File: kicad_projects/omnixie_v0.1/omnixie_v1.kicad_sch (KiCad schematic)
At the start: 67 parts, among them J1 Conn_01x10, J2 SM04B-SRSS-TB, J3 SM04B-SRSS-TB, J4 USB4105-GF-A, J5 Conn_01x04, J6 Conn_01x02, J8 IL-WX-16S-VF-B-E1000E, Q0 BSS123, Q1 BSS123, Q10 BSS123, Q11 BSS123, Q12 IPN50R1K4CEATMA1, Q2 BSS123, Q3 BSS123, Q4 BSS123, Q5 BSS123, Q6 BSS123, Q7 BSS123, Q8 BSS123, Q9 BSS123, T1 ATB322515-0110, U1 CH32V003F4U6, U3 PI4IOE5V6416ZDEX, U4 XC6206P332MR

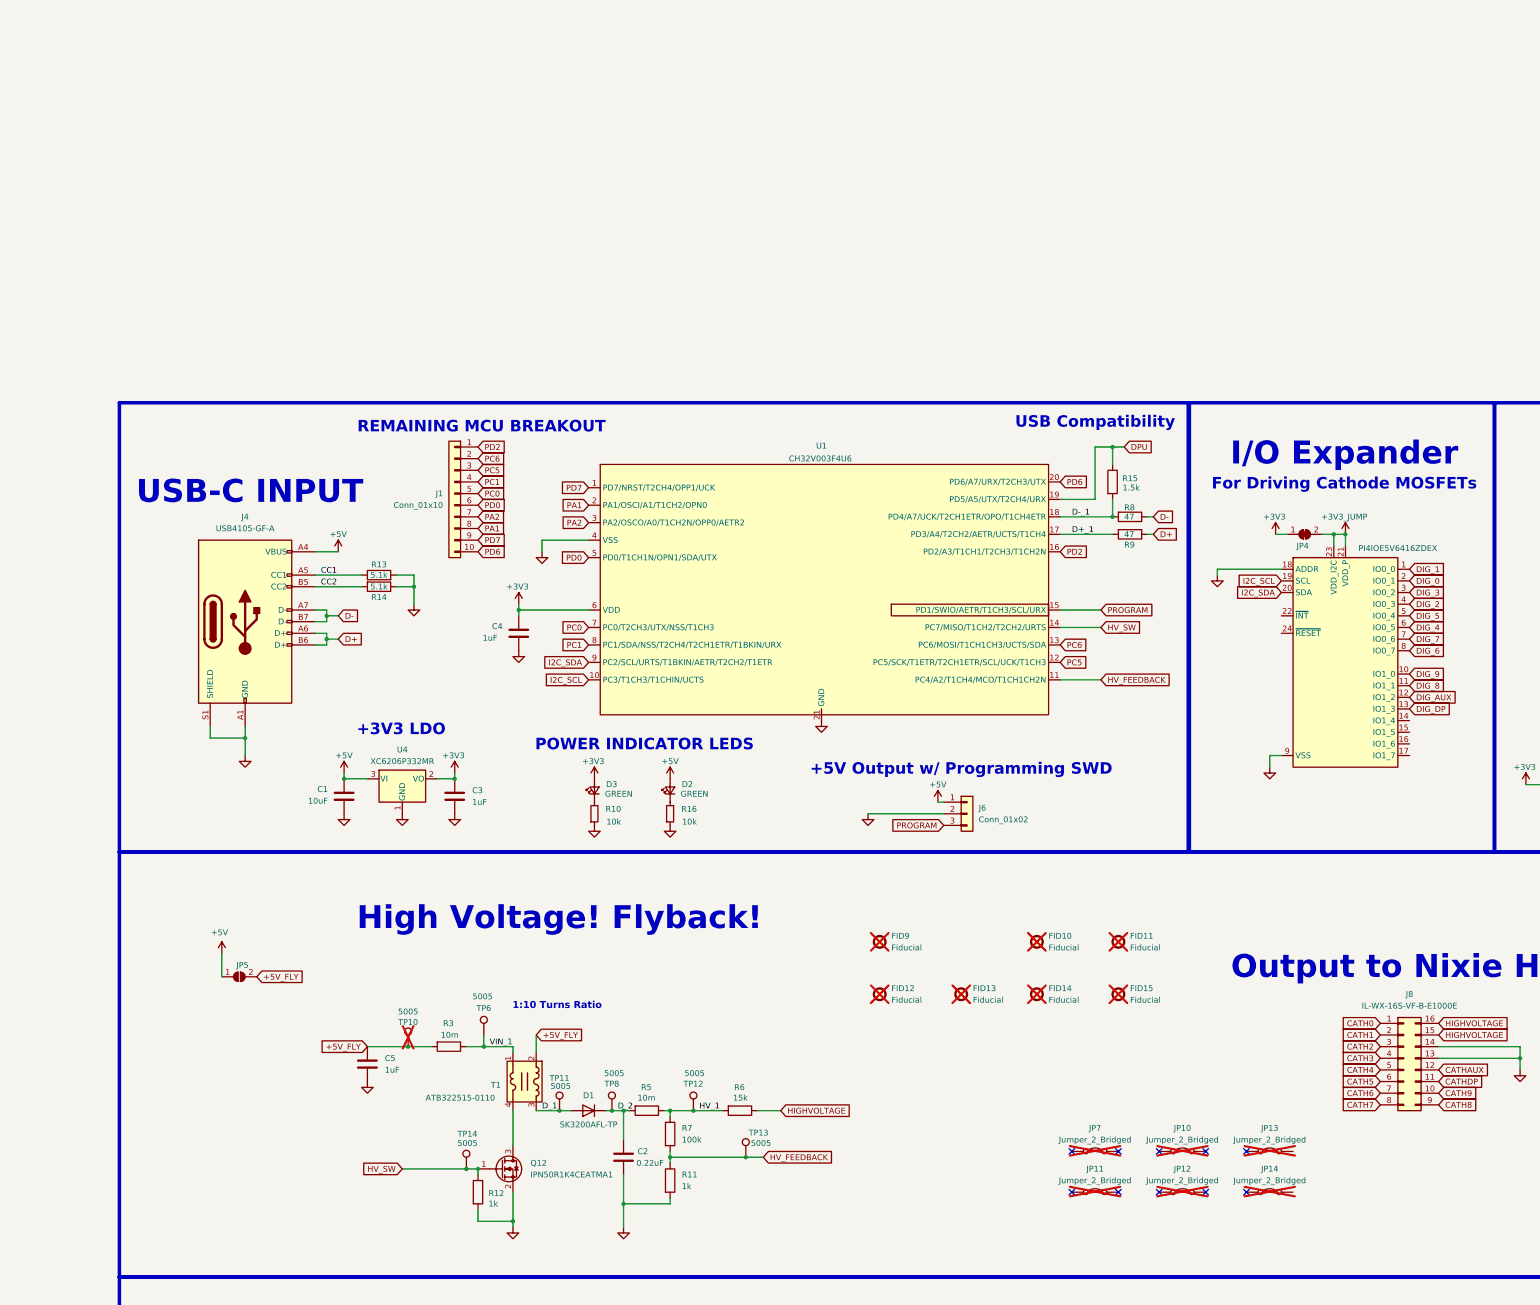
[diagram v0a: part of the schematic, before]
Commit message: removed unneccesary stuff
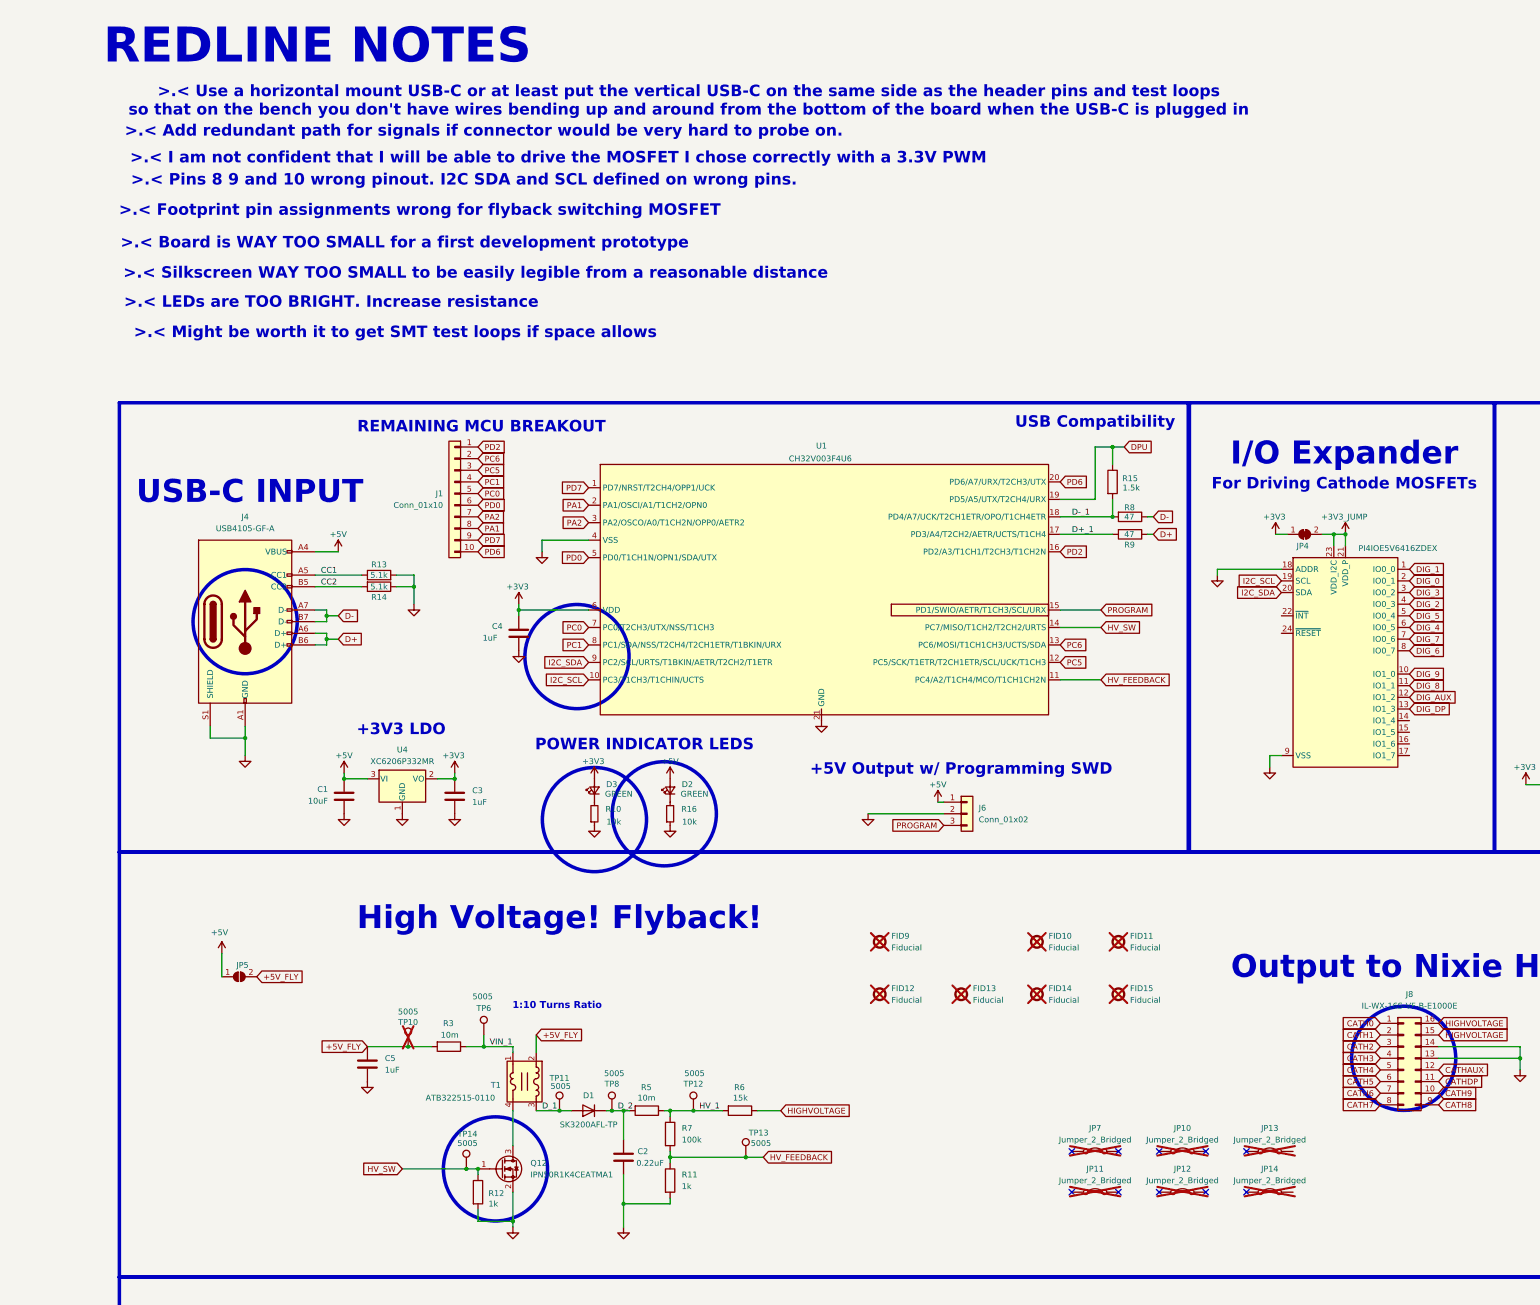
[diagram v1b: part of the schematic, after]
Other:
- note added: ">.< Add redundant path for signals if connector would be very hard to probe on."
- note added: ">.< Board is WAY TOO SMALL for a first development prototype"
- note added: ">.< Footprint pin assignments wrong for flyback switching MOSFET"
- note added: ">.< I am not confident that I will be able to drive the MOSFET I chose correctly with a 3.3V PWM"
- note added: ">.< LEDs are TOO BRIGHT. Increase resistance"
- note added: ">.< Might be worth it to get SMT test loops if space allows"
- note added: ">.< Pins 8 9 and 10 wrong pinout. I2C SDA and SCL defined on wrong pins."
- note added: ">.< Silkscreen WAY TOO SMALL to be easily legible from a reasonable distance"
- note added: ">.< Use a horizontal mount USB-C or at least put the vertical USB-C on the same side as the header pins and test loops so that on the bench you don't have wires bending up and around from the bottom of the board when the USB-C is plugged in"
- note added: "REDLINE NOTES"
